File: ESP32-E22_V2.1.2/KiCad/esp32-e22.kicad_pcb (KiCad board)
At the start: 2 copper layers, 70 x 99 mm, 46 parts, among them J1 Conn_01x02_Socket, J10 Conn_01x02_Socket, J11 Conn_01x04_Socket, J3 Screw_Terminal_01x02, J4 Conn_01x04_Socket, J5 Conn_01x03_Socket, J6 Conn_01x04_Socket, J7 Conn_01x05_Socket, J8 SMA, J9 Conn_01x02_Socket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

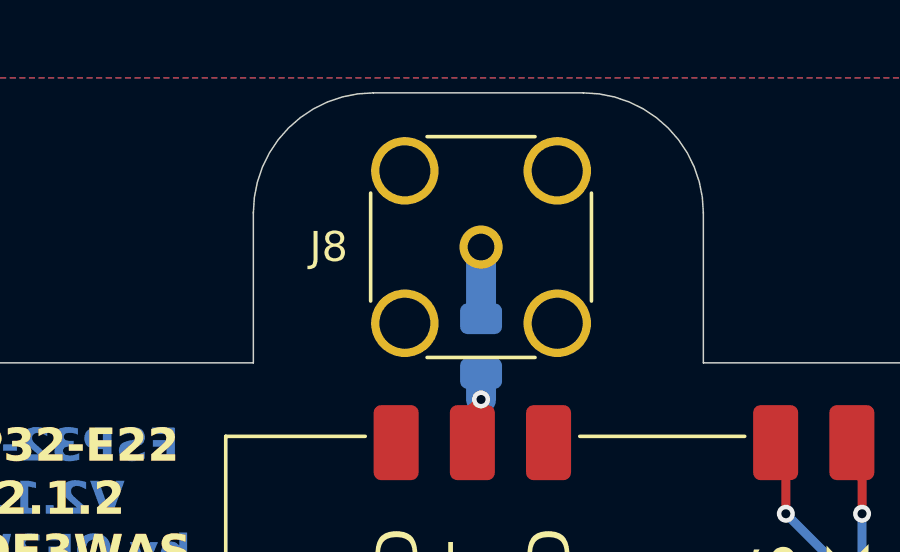
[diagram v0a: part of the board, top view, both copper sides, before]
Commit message: update Assembly
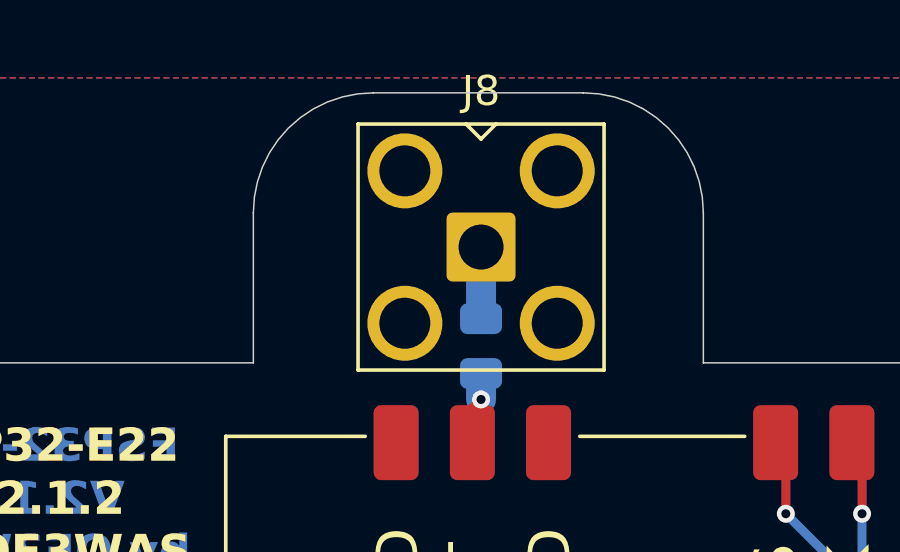
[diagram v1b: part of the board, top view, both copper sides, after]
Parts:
- J8: footprint Connector_Coaxial:SMA_Amphenol_132134-14_Vertical -> Connector_Coaxial:SMA_Amphenol_901-143_Horizontal
- turned J8 to -90 degrees

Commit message: PCB β3
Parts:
- added J12: Conn_01x02_Socket, Connector_PinHeader_2.54mm:PinHeader_1x02_P2.54mm_Horizontal, B.Cu at (137.2, 136.0)
- D5: footprint Diode_THT:D_DO-41_SOD81_P5.08mm_Vertical_KathodeUp -> Diode_THT:D_DO-41_SOD81_P2.54mm_Vertical_KathodeUp
- U1: value ESP32-DevKitC -> ESP32-DevKitC V4
- U3: value E22-40033S -> E22-400M33S
- moved J10 8.26 mm to (116.2, 120.0)
- moved SW1 3.81 mm to (113.0, 123.8)
- moved C3 2.62 mm to (165.1, 86.4), turned to -90 degrees
- moved J9 2.54 mm to (154.9, 86.4)
- moved D5 1.91 mm to (166.4, 127.6)
- moved C6 1.27 mm to (167.0, 123.2)
- moved F1 1.27 mm to (177.5, 121.3)
- moved J3 0.97 mm to (172.1, 129.5)
- moved J8 0.63 mm to (137.2, 51.4)
- moved D3 0.63 mm to (161.9, 123.2)
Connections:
- U4 pad 4: unconnected-(U4-EN-Pad4) -> Net-(J12-Pin_1)
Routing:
- net Net-(J12-Pin_1): track 0.00 -> 26.9 mm
- net Net-(J10-Pin_1): track 16.2 -> 20.3 mm
- net /E22_TXEN: track 66.4 -> 65.3 mm
- net /E22_RXEN: track 57.8 -> 56.7 mm
- net Net-(D5-K): track 22.0 -> 23.1 mm
- net Net-(J9-Pin_1): track 3.91 -> 4.68 mm
- net +5V: track 140.2 -> 139.4 mm
- net Net-(J8-In): track 2.39 -> 3.02 mm
- net GND: track 0.64 -> 1.23 mm
